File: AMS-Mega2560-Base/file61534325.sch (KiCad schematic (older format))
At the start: 10 parts, among them IC11 24PCDFA6D, IC12 24PCDFA6D, IC13 TL071CP, IC14 INA849DR, IC15 INA849DR, U2 TL431LP

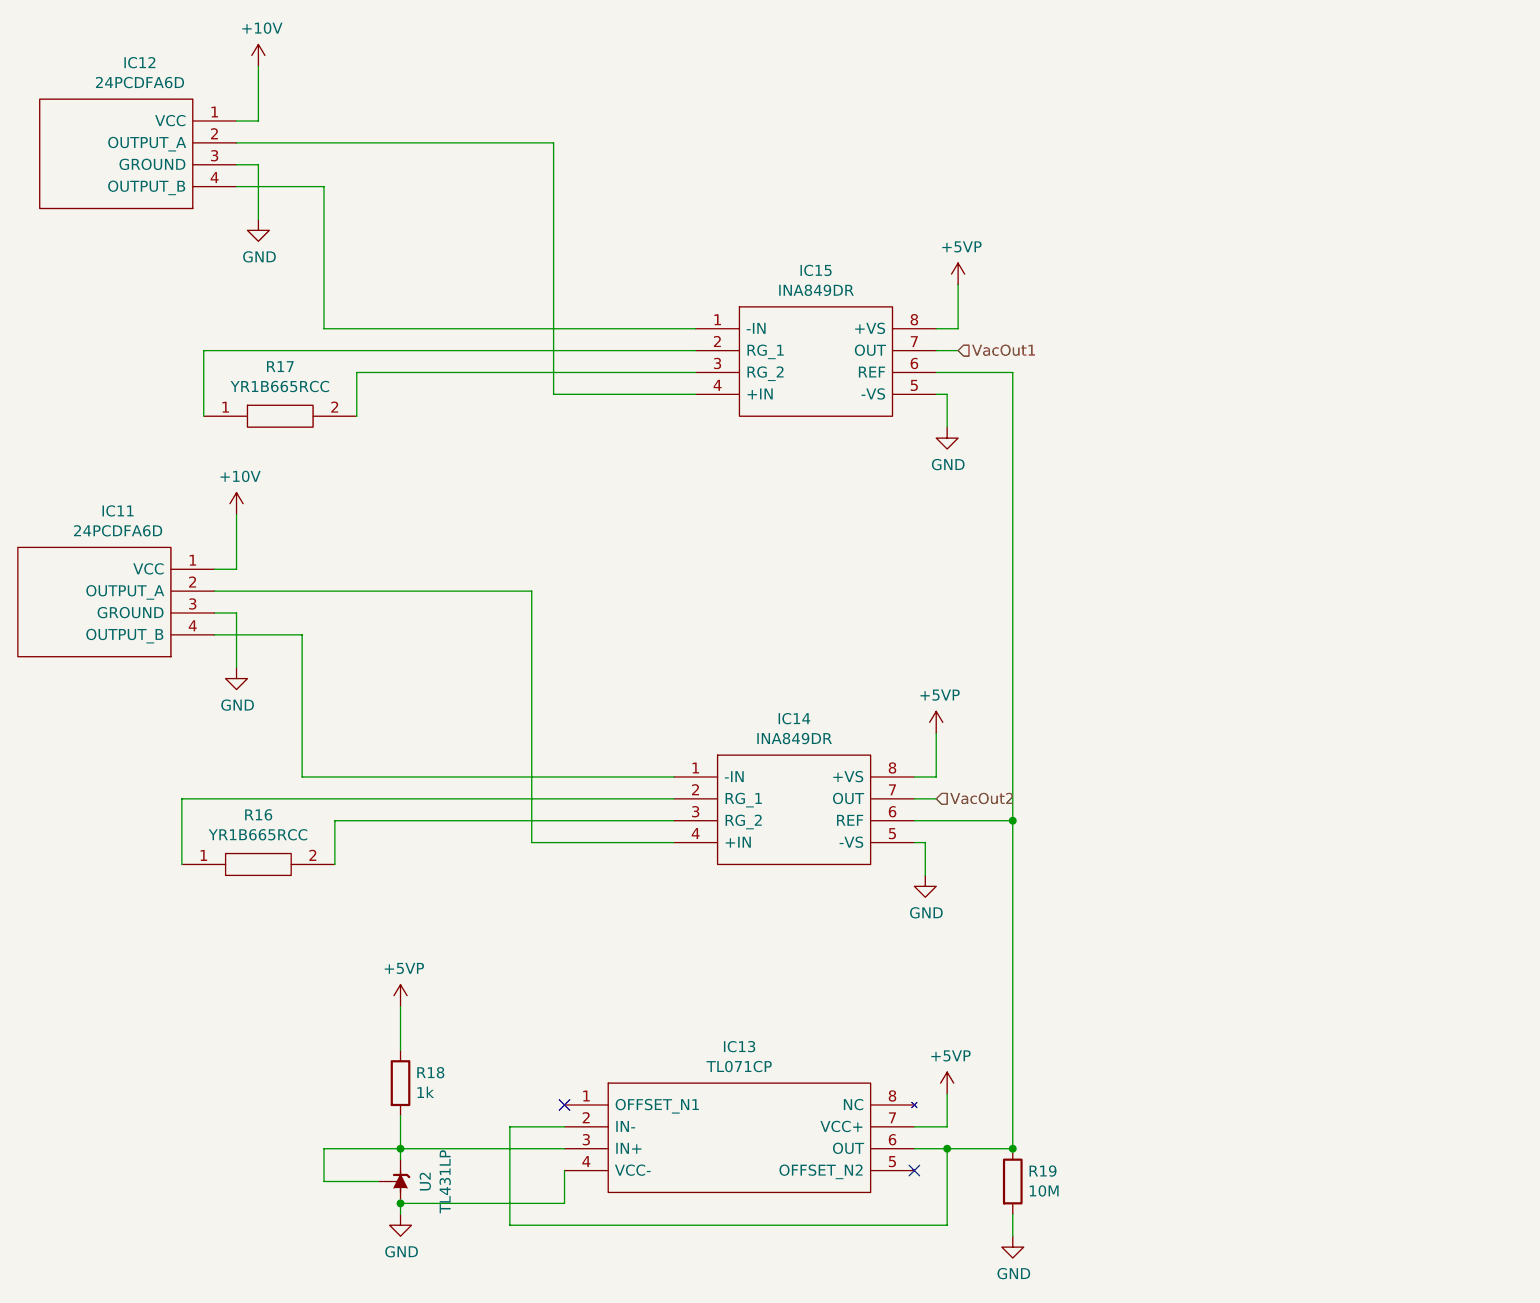
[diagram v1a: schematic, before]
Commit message: rearranging some of the hw design before i rename the repo.
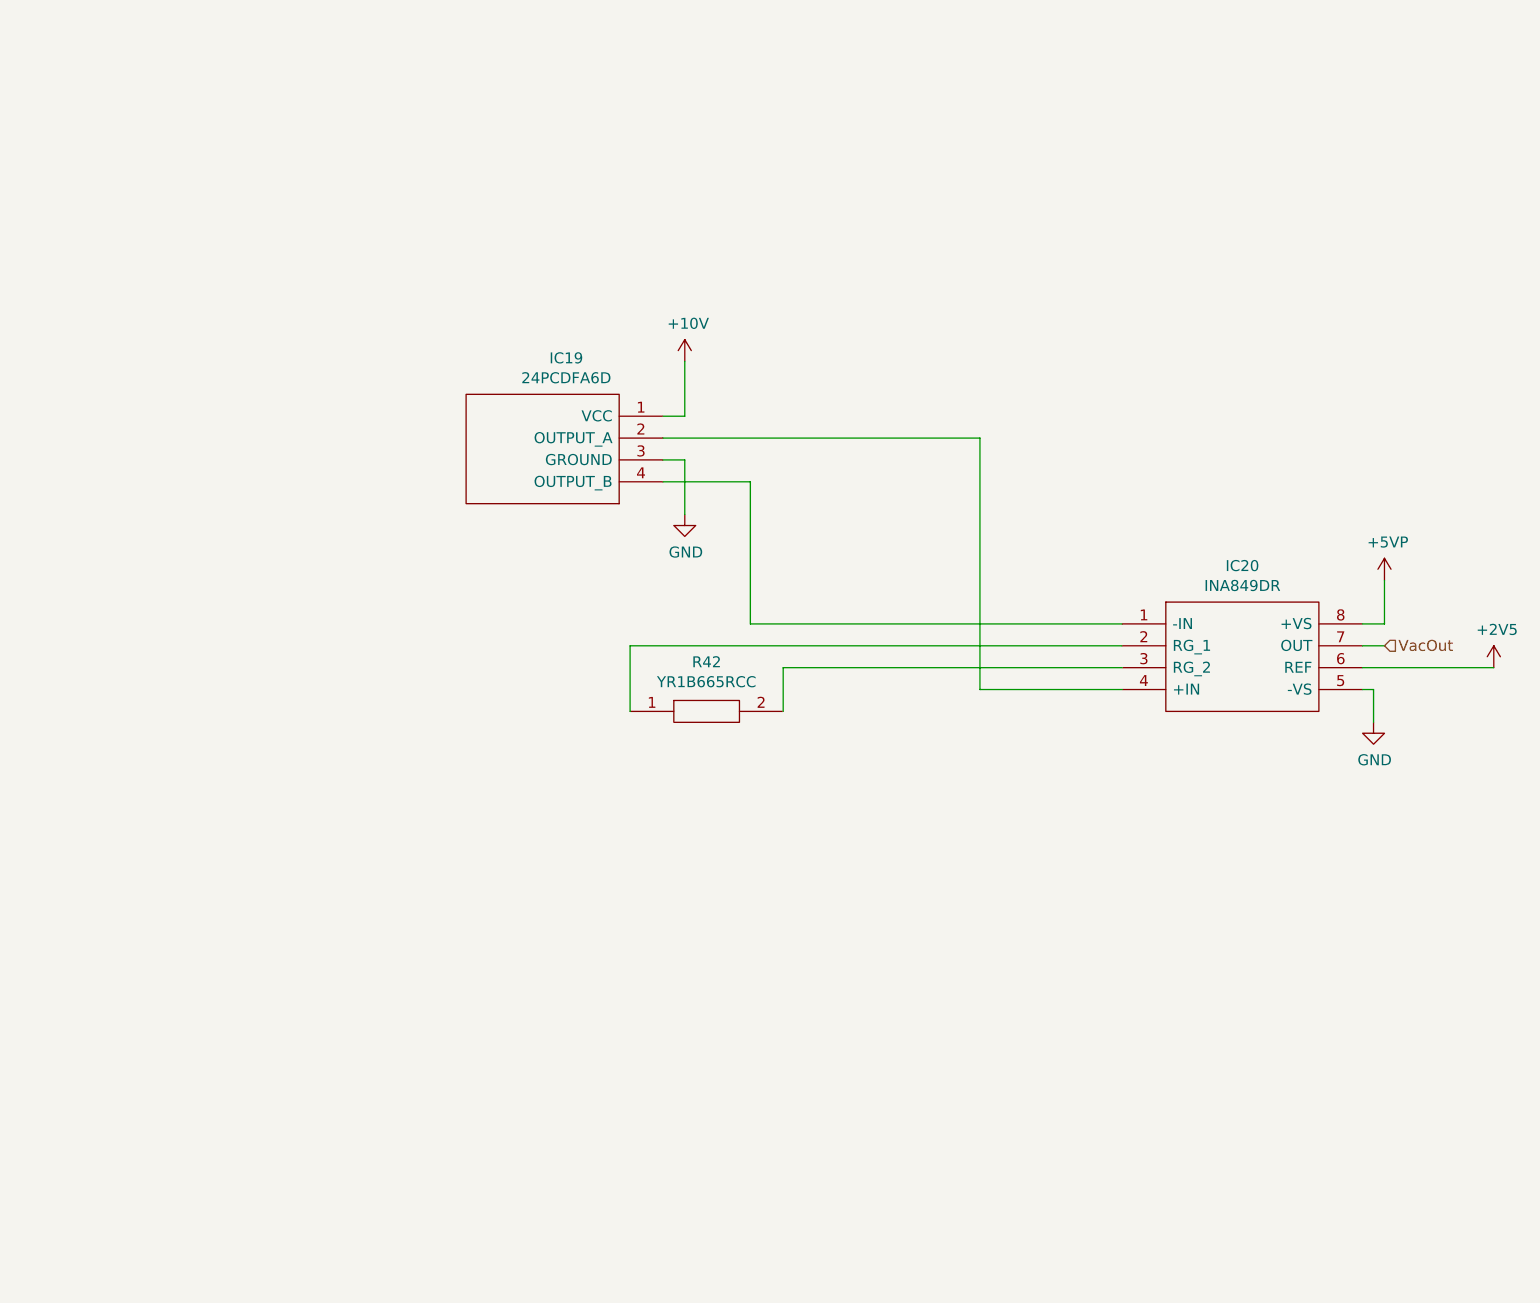
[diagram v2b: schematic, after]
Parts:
- removed IC11: 24PCDFA6D, SamacSys_Parts:24PCDFA6D, symbol SamacSys_Parts:24PCDFA6D
- removed IC13: TL071CP, SamacSys_Parts:DIP794W53P254L959H508Q8N, symbol SamacSys_Parts:TL071CP
- removed IC14: INA849DR, SamacSys_Parts:SOIC127P600X175-8N, symbol SamacSys_Parts:INA849DR
- removed R16: YR1B665RCC, SamacSys_Parts:RESAD1550W60L630D230, symbol SamacSys_Parts:YR1B665RCC
- removed R18: 1k, Resistor_THT:R_Axial_DIN0207_L6.3mm_D2.5mm_P5.08mm_Vertical, symbol Device:R
- removed R19: 10M, Resistor_THT:R_Axial_DIN0207_L6.3mm_D2.5mm_P5.08mm_Vertical, symbol Device:R
- removed U2: TL431LP, Package_TO_SOT_THT:TO-92_Inline, symbol Reference_Voltage:TL431LP
- renumbered IC12 to IC15, IC15 to IC16, R17 to R23
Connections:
- net +2V5: now reaches IC16.6 (REF)
- net VacOut1 renamed VacOut
- no-connect marks 2 -> 0
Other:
- moved on the sheet: IC19, IC20, R42
